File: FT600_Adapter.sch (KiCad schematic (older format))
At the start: 22 parts, among them J1 CX70M-24P1, J2 Conn_02x20_Odd_Even, U1 FT600Q-T, Y1 30MHz

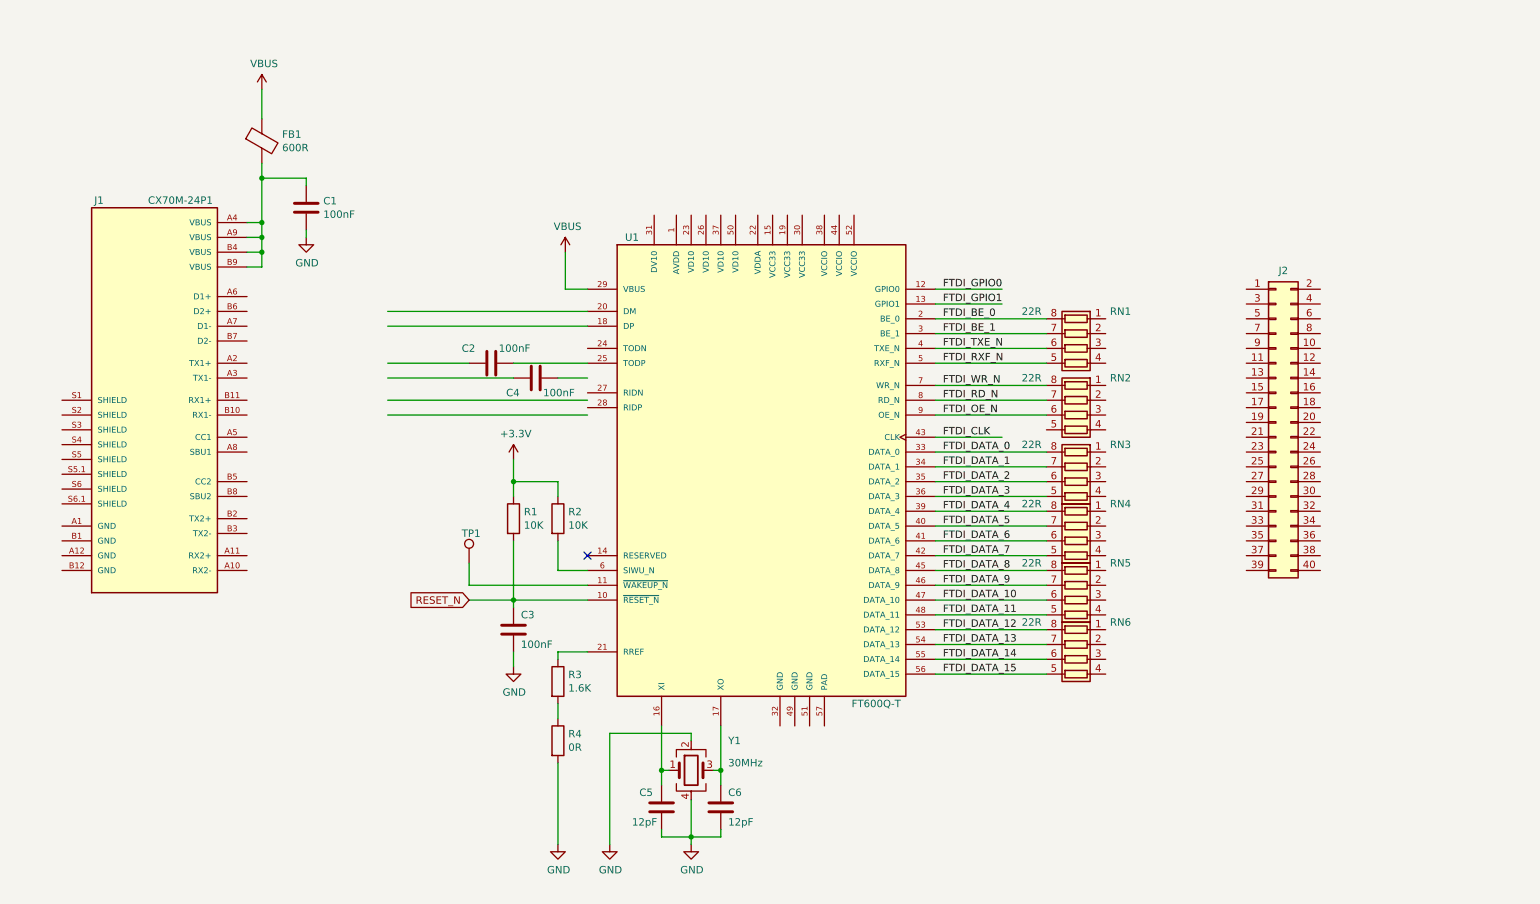
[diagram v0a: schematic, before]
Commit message: Updated USB3.0 connector
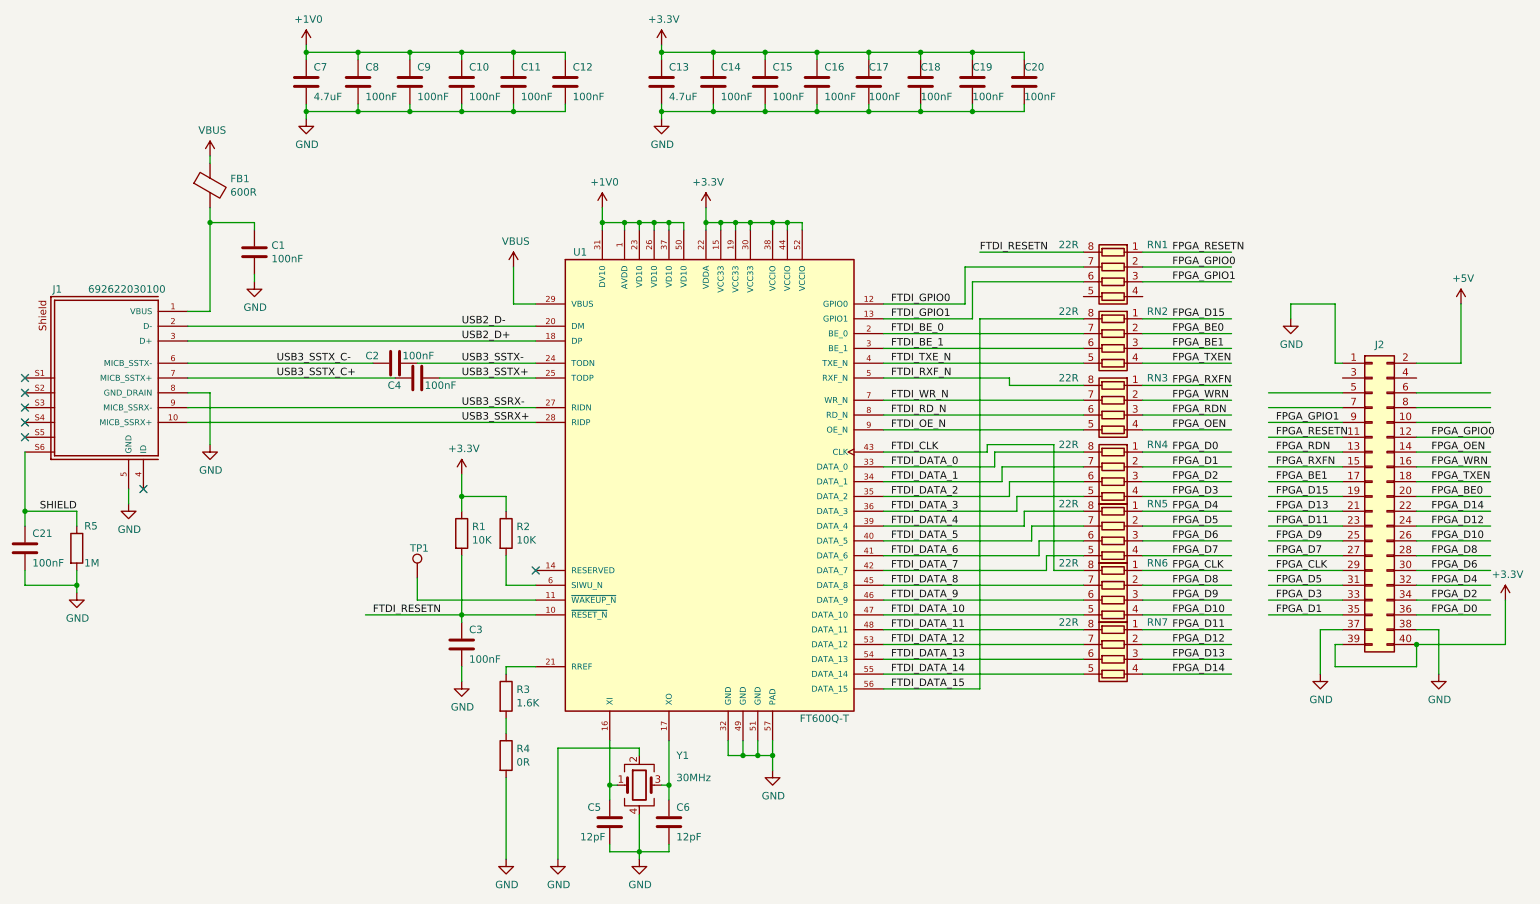
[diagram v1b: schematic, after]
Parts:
- removed J1: CX70M-24P1, HRS_CX70M-24P1, symbol CX70M-24P1:CX70M-24P1
- added C10, C11, C12, C14, C15, C16, C17, C18, C19, C20, C21, C8, C9: 100nF, Capacitor_SMD:C_0402_1005Metric, symbol Device:C
- added C13, C7: 4.7uF, Capacitor_SMD:C_0603_1608Metric, symbol Device:C
- added J1: 692622030100, 692622030100, symbol 692622030100:692622030100
- added R5: 1M, Resistor_SMD:R_0402_1005Metric, symbol Device:R
- added RN1: 22R, Resistor_SMD:R_Array_Convex_4x0402, symbol Device:R_Pack04
- renumbered RN1 to RN2, RN2 to RN3, RN3 to RN4, RN4 to RN5, RN5 to RN6, RN6 to RN7
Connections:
- net labels added: +1V0, +5V, FPGA_BE0, FPGA_BE1, FPGA_CLK, FPGA_D0, FPGA_D1, FPGA_D10, FPGA_D11, FPGA_D12, FPGA_D13, FPGA_D14, FPGA_D15, FPGA_D2, FPGA_D3, FPGA_D4, FPGA_D5, FPGA_D6, FPGA_D7, FPGA_D8, FPGA_D9, FPGA_GPIO0, FPGA_GPIO1, FPGA_OEN, FPGA_RDN, FPGA_RESETN, FPGA_RXFN, FPGA_TXEN, FPGA_WRN, FTDI_RESETN, SHIELD, USB2_D+, USB2_D-, USB3_SSRX+, USB3_SSRX-, USB3_SSTX+, USB3_SSTX-, USB3_SSTX_C+, USB3_SSTX_C-
- net labels removed: RESET_N
- wire segments 81 -> 280
- no-connect marks 1 -> 7
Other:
- moved on the sheet: C1, C2, C3, C4, C5, C6, FB1, J2, R1, R2, R3, R4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

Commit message: Updated PCB layout
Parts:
- added D1: GREEN, LED_SMD:LED_0603_1608Metric, symbol Device:LED
- added R6: 10K, Resistor_SMD:R_0402_1005Metric, symbol Device:R
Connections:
- net labels added: CONN_VBUS
- wire segments 280 -> 284
- no-connect marks 7 -> 8
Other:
- moved on the sheet: C1, FB1
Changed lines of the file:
@@
 encoding utf-8
 Sheet 1 1
-Title ""
-Date ""
-Rev ""
+Title "FT600 ADAPTER"
+Date "2021-01-01"
+Rev "A"
 Comp ""
 Comment1 ""
@@
 L Device:Ferrite_Bead FB1
 U 1 1 5FE8AA8D
-P 2150 1950
-F 0 "FB1" H 2287 1996 50  0000 L CNN
-F 1 "600R" H 2287 1905 50  0000 L CNN
-F 2 "Inductor_SMD:L_0603_1608Metric" V 2080 1950 50  0001 C CNN
-F 3 "MPZ1608S601ATA00" H 2150 1950 50  0001 C CNN
-	1    2150 1950
+P 2500 2000
+F 0 "FB1" H 2637 2046 50  0000 L CNN
+F 1 "600R" H 2637 1955 50  0000 L CNN
+F 2 "Inductor_SMD:L_0603_1608Metric" V 2430 2000 50  0001 C CNN
+F 3 "MPZ1608S601ATA00" H 2500 2000 50  0001 C CNN
+	1    2500 2000
 	1    0    0    -1
 $EndComp
@@
 L Device:C C1
 U 1 1 5FE8C4C3
-P 2450 2400
-F 0 "C1" H 2565 2446 50  0000 L CNN
-F 1 "100nF" H 2565 2355 50  0000 L CNN
-F 2 "Capacitor_SMD:C_0402_1005Metric" H 2488 2250 50  0001 C CNN
-F 3 "~" H 2450 2400 50  0001 C CNN
-F 4 "GCM155R71C104KA55D" H 2450 2400 50  0001 C CNN "Part"
-	1    2450 2400
+P 2750 2400
+F 0 "C1" H 2865 2446 50  0000 L CNN
+F 1 "100nF" H 2865 2355 50  0000 L CNN
+F 2 "Capacitor_SMD:C_0402_1005Metric" H 2788 2250 50  0001 C CNN
+F 3 "~" H 2750 2400 50  0001 C CNN
+F 4 "GCM155R71C104KA55D" H 2750 2400 50  0001 C CNN "Part"
+	1    2750 2400
 	1    0    0    -1
 $EndComp
@@
 $EndComp
 Wire Wire Line
-	2450 2250 2450 2200
-Wire Wire Line
-	2450 2200 2150 2200
-Wire Wire Line
-	2150 2200 2150 2100
-Wire Wire Line
-	2450 2600 2450 2550
+	2750 2250 2750 2200
+Wire Wire Line
+	2750 2200 2500 2200
+Wire Wire Line
+	2500 2200 2500 2150
+Wire Wire Line
+	2750 2600 2750 2550
 $Comp
 L power:GND #PWR0101
 U 1 1 5FE948F2
-P 2450 2600
-F 0 "#PWR0101" H 2450 2350 50  0001 C CNN
-F 1 "GND" H 2455 2427 50  0000 C CNN
-F 2 "" H 2450 2600 50  0001 C CNN
-F 3 "" H 2450 2600 50  0001 C CNN
-	1    2450 2600
+P 2750 2600
+F 0 "#PWR0101" H 2750 2350 50  0001 C CNN
+F 1 "GND" H 2755 2427 50  0000 C CNN
+F 2 "" H 2750 2600 50  0001 C CNN
+F 3 "" H 2750 2600 50  0001 C CNN
+	1    2750 2600
 	1    0    0    -1
 $EndComp
@@
 L power:VBUS #PWR0102
 U 1 1 5FE96419
-P 2150 1750
-F 0 "#PWR0102" H 2150 1600 50  0001 C CNN
-F 1 "VBUS" H 2165 1923 50  0000 C CNN
-F 2 "" H 2150 1750 50  0001 C CNN
-F 3 "" H 2150 1750 50  0001 C CNN
-	1    2150 1750
-	1    0    0    -1
-$EndComp
-Wire Wire Line
-	2150 1750 2150 1800
+P 2500 1800
+F 0 "#PWR0102" H 2500 1650 50  0001 C CNN
+F 1 "VBUS" H 2515 1973 50  0000 C CNN
+F 2 "" H 2500 1800 50  0001 C CNN
+F 3 "" H 2500 1800 50  0001 C CNN
+	1    2500 1800
+	1    0    0    -1
+$EndComp
+Wire Wire Line
+	2500 1800 2500 1850
 $Comp
 L power:VBUS #PWR0103
@@
 Wire Wire Line
 	10300 3550 10800 3550
-Wire Wire Line
-	9800 3450 9300 3450
-Wire Wire Line
-	10300 3450 10800 3450
-Wire Wire Line
-	9800 3350 9300 3350
-Wire Wire Line
-	10300 3350 10800 3350
 Text Label 10400 4050 0    50   ~ 0
 FPGA_BE0
@@
 USB3_SSTX_C+
 Wire Wire Line
-	2150 2200 2150 2800
-Wire Wire Line
-	2150 2800 2000 2800
-Connection ~ 2150 2200
+	2500 2200 2500 2800
+Connection ~ 2500 2200
 Wire Wire Line
 	2000 2900 4350 2900
@@
 U 1 1 6097C8D3
 P 1250 4400
-F 0 "R5" H 1300 4550 50  0000 L CNN
+F 0 "R5" H 1300 4500 50  0000 L CNN
 F 1 "1M" H 1300 4300 50  0000 L CNN
 F 2 "Resistor_SMD:R_0402_1005Metric" V 1180 4400 50  0001 C CNN
@@
 	900  4150 900  3750
 Connection ~ 900  4150
-NoConn ~ 900  3650
-NoConn ~ 900  3550
-NoConn ~ 900  3450
-NoConn ~ 900  3350
-NoConn ~ 900  3250
 $Comp
 L power:GND #PWR0120
@@
 Wire Wire Line
 	5750 5800 5850 5800
+Text Label 2000 2800 0    50   ~ 0
+CONN_VBUS
+Wire Wire Line
+	2000 2800 2500 2800
+Wire Wire Line
+	900  3250 900  3350
+Connection ~ 900  3750
+Connection ~ 900  3350
+Wire Wire Line
+	900  3350 900  3450
+Connection ~ 900  3450
+Wire Wire Line
+	900  3450 900  3550
+Connection ~ 900  3550
+Wire Wire Line
+	900  3550 900  3650
+Connection ~ 900  3650
+Wire Wire Line
+	900  3650 900  3750
+$Comp
+L Device:LED D1
+U 1 1 6059BF45
+P 9750 2100
+F 0 "D1" V 9789 1982 50  0000 R CNN
+F 1 "GREEN" V 9698 1982 50  0000 R CNN
+F 2 "LED_SMD:LED_0603_1608Metric" H 9750 2100 50  0001 C CNN
+F 3 "~" H 9750 2100 50  0001 C CNN
+	1    9750 2100
+	0    -1   -1   0
+$EndComp
+$Comp
+L Device:R R6
+U 1 1 605CCD9A
+P 9750 1750
+F 0 "R6" H 9820 1796 50  0000 L CNN
+F 1 "10K" H 9820 1705 50  0000 L CNN
+F 2 "Resistor_SMD:R_0402_1005Metric" V 9680 1750 50  0001 C CNN
+F 3 "~" H 9750 1750 50  0001 C CNN
+	1    9750 1750
+	1    0    0    -1
+$EndComp
+$Comp
+L power:GND #PWR0124
+U 1 1 605CDDA5
+P 9750 2350
+F 0 "#PWR0124" H 9750 2100 50  0001 C CNN
+F 1 "GND" H 9755 2177 50  0000 C CNN
+F 2 "" H 9750 2350 50  0001 C CNN
+F 3 "" H 9750 2350 50  0001 C CNN
+	1    9750 2350
+	1    0    0    -1
+$EndComp
+Wire Wire Line
+	9750 2250 9750 2350
+$Comp
+L power:+5V #PWR0125
+U 1 1 60618348
+P 9750 1500
+F 0 "#PWR0125" H 9750 1350 50  0001 C CNN
+F 1 "+5V" H 9765 1673 50  0000 C CNN
+F 2 "" H 9750 1500 50  0001 C CNN
+F 3 "" H 9750 1500 50  0001 C CNN
+	1    9750 1500
+	1    0    0    -1
+$EndComp
+Wire Wire Line
+	9750 1900 9750 1950
+Wire Wire Line
+	9750 1500 9750 1600
+NoConn ~ 10300 3250
+NoConn ~ 10300 3350
+NoConn ~ 10300 3450
+NoConn ~ 9800 3450
+NoConn ~ 9800 3350
+NoConn ~ 9800 3250
 $EndSCHEMATC

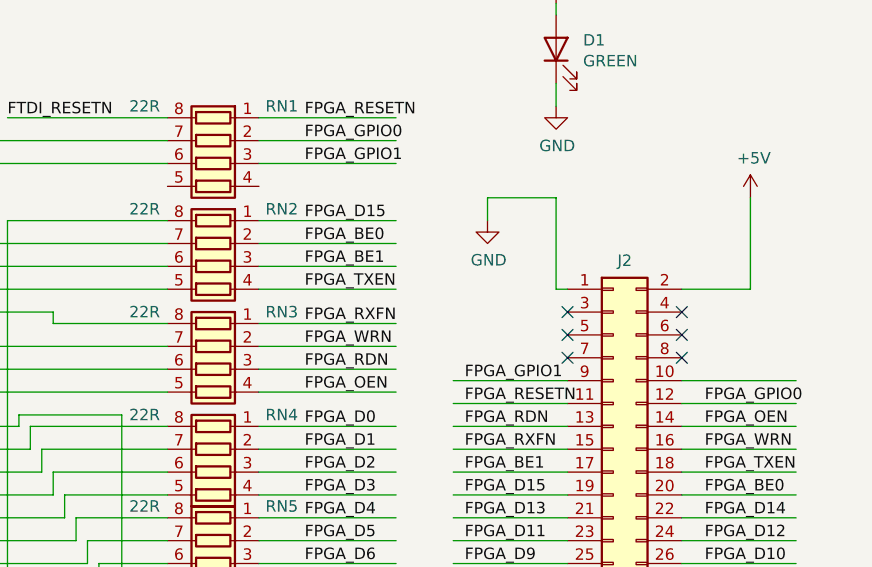
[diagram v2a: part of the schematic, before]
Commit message: Removed unused nets
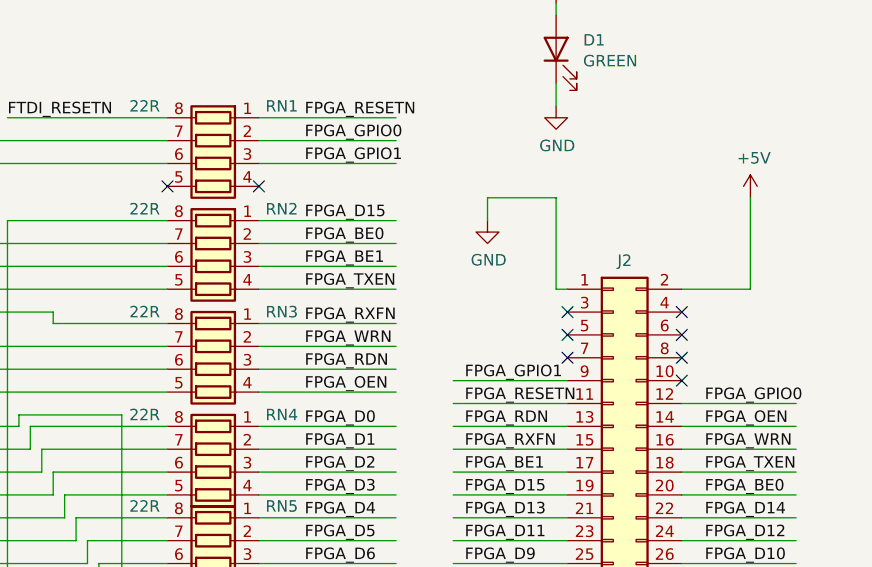
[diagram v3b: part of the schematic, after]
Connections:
- wire segments 284 -> 283
- no-connect marks 8 -> 11
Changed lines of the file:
@@
 Wire Wire Line
 	9800 3550 9300 3550
-Wire Wire Line
-	10300 3550 10800 3550
 Text Label 10400 4050 0    50   ~ 0
 FPGA_BE0
@@
 Text Label 10400 3750 0    50   ~ 0
 FPGA_OEN
-$Comp
-L Device:R_Pack04 RN1
-U 1 1 601914E3
-P 8250 2600
-F 0 "RN1" V 8000 2300 50  0000 C CNN
-F 1 "22R" V 8000 2900 50  0000 C CNN
-F 2 "Resistor_SMD:R_Array_Convex_4x0402" V 8525 2600 50  0001 C CNN
-F 3 "~" H 8250 2600 50  0001 C CNN
-F 4 "YC124-FR-0722RL" V 8250 2600 50  0001 C CNN "Part"
-	1    8250 2600
-	0    -1   1    0
-$EndComp
 Wire Wire Line
 	6700 2750 7250 2750
@@
 NoConn ~ 9800 3350
 NoConn ~ 9800 3250
+NoConn ~ 10300 3550
+NoConn ~ 8450 2700
+$Comp
+L Device:R_Pack04 RN1
+U 1 1 601914E3
+P 8250 2600
+F 0 "RN1" V 8000 2300 50  0000 C CNN
+F 1 "22R" V 8000 2900 50  0000 C CNN
+F 2 "Resistor_SMD:R_Array_Convex_4x0402" V 8525 2600 50  0001 C CNN
+F 3 "~" H 8250 2600 50  0001 C CNN
+F 4 "YC124-FR-0722RL" V 8250 2600 50  0001 C CNN "Part"
+	1    8250 2600
+	0    -1   1    0
+$EndComp
+NoConn ~ 8050 2700
 $EndSCHEMATC
